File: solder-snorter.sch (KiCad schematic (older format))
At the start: 15 parts, among them J1 USB_B_Micro, M1 Fan, U1 MCP73831, U2 TLV61046A

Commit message: Footprints done; layout started
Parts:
- removed SW?: SW_SPST, symbol Switch:SW_SPST
- added SW1: SW_SPDT, solder-snorter:SW_SPDT_OS102011MA1QN1, symbol Switch:SW_SPDT
- BT1: footprint (none) -> solder-snorter:BatteryHolder_Keystone_54_1x18650; MPN (none) -> Keystone 54 (x 2)
- C1, C2: footprint (none) -> Capacitor_SMD:C_0805_2012Metric_Pad1.15x1.40mm_HandSolder; MPN (none) -> 0805X475M250CT
- C3: footprint (none) -> Capacitor_SMD:C_0805_2012Metric_Pad1.15x1.40mm_HandSolder; MPN (none) -> 0805X225M160CT
- C4: footprint (none) -> Capacitor_SMD:C_0805_2012Metric_Pad1.15x1.40mm_HandSolder; MPN (none) -> C0805C106K4PAC
- D1, D2: footprint (none) -> LED_SMD:LED_0805_2012Metric_Pad1.15x1.40mm_HandSolder
- J1: footprint (none) -> solder-snorter:USB_Micro-B_Amphenol_10118194-0001LF; MPN (none) -> 10118194-0001LF
- L1: footprint (none) -> solder-snorter:L_Murata_FDSD0420-H-100M; MPN (none) -> FDSD0420-H-100M=P3
- M1: footprint (none) -> Connector_PinSocket_2.54mm:PinSocket_1x02_P2.54mm_Vertical; MPN (none) -> CFM-8025V-132-330
- R1, R2: footprint (none) -> Resistor_SMD:R_0805_2012Metric_Pad1.15x1.40mm_HandSolder
- U1: footprint (none) -> Package_TO_SOT_SMD:SOT-23-5_HandSoldering; MPN (none) -> MCP73831T-2ACI/OT
- U2: footprint (none) -> Package_TO_SOT_SMD:SOT-23-6_Handsoldering; MPN (none) -> TLV61046ADBVR
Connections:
- net GND: no longer J1.6 (Shield)
- net VBAT: now also SW1.2 (B)
- net VBATSW: now also SW1.3 (C)
- no-connect marks 3 -> 4
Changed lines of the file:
@@
 F 0 "U1" H 4550 1940 50  0000 C CNN
 F 1 "MCP73831" H 4550 1849 50  0000 C CNN
-F 2 "" H 4550 1475 50  0001 C CNN
-F 3 "" H 4550 1475 50  0001 C CNN
+F 2 "Package_TO_SOT_SMD:SOT-23-5_HandSoldering" H 4550 1475 50  0001 C CNN
+F 3 "https://www.mouser.at/datasheet/2/268/20001984g-846362.pdf" H 4550 1475 50  0001 C CNN
+F 4 "MCP73831T-2ACI/OT" H 4550 1475 50  0001 C CNN "MPN"
 	1    4550 1475
 	1    0    0    -1
@@
 F 0 "J1" H 2307 1942 50  0000 C CNN
 F 1 "USB_B_Micro" H 2307 1851 50  0000 C CNN
-F 2 "" H 2400 1425 50  0001 C CNN
-F 3 "~" H 2400 1425 50  0001 C CNN
+F 2 "solder-snorter:USB_Micro-B_Amphenol_10118194-0001LF" H 2400 1425 50  0001 C CNN
+F 3 "https://cdn.amphenol-icc.com/media/wysiwyg/files/drawing/10118194.pdf" H 2400 1425 50  0001 C CNN
+F 4 "10118194-0001LF" H 2250 1475 50  0001 C CNN "MPN"
 	1    2250 1475
 	1    0    0    -1
@@
 	1    0    0    -1
 $EndComp
-Wire Wire Line
-	2250 1875 2250 1925
-Wire Wire Line
-	2150 1875 2150 1925
-Wire Wire Line
-	2150 1925 2250 1925
-Connection ~ 2250 1925
-Wire Wire Line
-	2250 1925 2250 2025
 NoConn ~ 2550 1475
 NoConn ~ 2550 1575
@@
 F 0 "C1" H 3065 1696 50  0000 L CNN
 F 1 "4.7U" H 3065 1605 50  0000 L CNN
-F 2 "" H 2988 1500 50  0001 C CNN
-F 3 "~" H 2950 1650 50  0001 C CNN
+F 2 "Capacitor_SMD:C_0805_2012Metric_Pad1.15x1.40mm_HandSolder" H 2988 1500 50  0001 C CNN
+F 3 "https://www.mouser.at/datasheet/2/210/WTC_MLCC_General_Purpose-1534899.pdf" H 2950 1650 50  0001 C CNN
+F 4 "0805X475M250CT" H 2950 1650 50  0001 C CNN "MPN"
 	1    2950 1650
 	1    0    0    -1
@@
 F 0 "BT1" H 6343 1646 50  0000 L CNN
 F 1 "Battery_Cell" H 6343 1555 50  0000 L CNN
-F 2 "" V 6225 1610 50  0001 C CNN
-F 3 "~" V 6225 1610 50  0001 C CNN
+F 2 "solder-snorter:BatteryHolder_Keystone_54_1x18650" V 6225 1610 50  0001 C CNN
+F 3 "https://www.mouser.at/datasheet/2/215/4-745936.pdf" V 6225 1610 50  0001 C CNN
+F 4 "Keystone 54 (x 2)" H 6225 1550 50  0001 C CNN "MPN"
 	1    6225 1550
 	1    0    0    -1
@@
 F 0 "R2" H 5245 1771 50  0000 L CNN
 F 1 "2K" H 5245 1680 50  0000 L CNN
-F 2 "" V 5105 1725 50  0001 C CNN
+F 2 "Resistor_SMD:R_0805_2012Metric_Pad1.15x1.40mm_HandSolder" V 5105 1725 50  0001 C CNN
 F 3 "~" H 5175 1725 50  0001 C CNN
 	1    5175 1725
@@
 F 0 "D1" H 3725 1450 50  0000 C CNN
 F 1 "LED" H 3700 1525 50  0000 C CNN
-F 2 "" H 3550 1575 50  0001 C CNN
+F 2 "LED_SMD:LED_0805_2012Metric_Pad1.15x1.40mm_HandSolder" H 3550 1575 50  0001 C CNN
 F 3 "~" H 3550 1575 50  0001 C CNN
 	1    3550 1575
@@
 F 0 "D2" H 3675 1750 50  0000 C CNN
 F 1 "LED" H 3700 1675 50  0000 C CNN
-F 2 "" H 3550 1800 50  0001 C CNN
+F 2 "LED_SMD:LED_0805_2012Metric_Pad1.15x1.40mm_HandSolder" H 3550 1800 50  0001 C CNN
 F 3 "~" H 3550 1800 50  0001 C CNN
 	1    3550 1800
@@
 F 0 "R1" V 3768 1675 50  0000 C CNN
 F 1 "470" V 3859 1675 50  0000 C CNN
-F 2 "" V 3905 1675 50  0001 C CNN
+F 2 "Resistor_SMD:R_0805_2012Metric_Pad1.15x1.40mm_HandSolder" V 3905 1675 50  0001 C CNN
 F 3 "~" H 3975 1675 50  0001 C CNN
 	1    3975 1675
@@
 F 0 "C2" H 5665 1696 50  0000 L CNN
 F 1 "4.7U" H 5665 1605 50  0000 L CNN
-F 2 "" H 5588 1500 50  0001 C CNN
-F 3 "~" H 5550 1650 50  0001 C CNN
+F 2 "Capacitor_SMD:C_0805_2012Metric_Pad1.15x1.40mm_HandSolder" H 5588 1500 50  0001 C CNN
+F 3 "https://www.mouser.at/datasheet/2/210/WTC_MLCC_General_Purpose-1534899.pdf" H 5550 1650 50  0001 C CNN
+F 4 "0805X475M250CT" H 5550 1650 50  0001 C CNN "MPN"
 	1    5550 1650
 	1    0    0    -1
@@
 F 0 "L1" V 4715 3575 50  0000 C CNN
 F 1 "10U" V 4624 3575 50  0000 C CNN
-F 2 "" H 4525 3575 50  0001 C CNN
-F 3 "~" H 4525 3575 50  0001 C CNN
+F 2 "solder-snorter:L_Murata_FDSD0420-H-100M" H 4525 3575 50  0001 C CNN
+F 3 "https://search.murata.co.jp/Ceramy/image/img/P02/J(E)TE243B-0001_FDSD0420_reference.pdf" H 4525 3575 50  0001 C CNN
+F 4 "FDSD0420-H-100M=P3" H 4525 3575 50  0001 C CNN "MPN"
 	1    4525 3575
 	0    -1   -1   0
@@
 F 0 "C3" H 3665 4521 50  0000 L CNN
 F 1 "2.2U" H 3665 4430 50  0000 L CNN
-F 2 "" H 3588 4325 50  0001 C CNN
-F 3 "~" H 3550 4475 50  0001 C CNN
+F 2 "Capacitor_SMD:C_0805_2012Metric_Pad1.15x1.40mm_HandSolder" H 3588 4325 50  0001 C CNN
+F 3 "https://www.mouser.at/datasheet/2/210/WTC_MLCC_General_Purpose-1534899.pdf" H 3550 4475 50  0001 C CNN
+F 4 "0805X225M160CT" H 3550 4475 50  0001 C CNN "MPN"
 	1    3550 4475
 	1    0    0    -1
@@
 F 0 "C4" H 5465 4521 50  0000 L CNN
 F 1 "10U" H 5465 4430 50  0000 L CNN
-F 2 "" H 5388 4325 50  0001 C CNN
-F 3 "~" H 5350 4475 50  0001 C CNN
+F 2 "Capacitor_SMD:C_0805_2012Metric_Pad1.15x1.40mm_HandSolder" H 5388 4325 50  0001 C CNN
+F 3 "https://www.mouser.at/datasheet/2/212/KEM_C1006_X5R_SMD-1103249.pdf" H 5350 4475 50  0001 C CNN
+F 4 "C0805C106K4PAC" H 5350 4475 50  0001 C CNN "MPN"
 	1    5350 4475
 	1    0    0    -1
@@
 F 0 "U2" H 4525 4715 50  0000 C CNN
 F 1 "TLV61046A" H 4525 4624 50  0000 C CNN
-F 2 "" H 4525 4250 79  0001 C CNN
-F 3 "" H 4525 4250 79  0001 C CNN
+F 2 "Package_TO_SOT_SMD:SOT-23-6_Handsoldering" H 4525 4250 79  0001 C CNN
+F 3 "http://www.ti.com/general/docs/suppproductinfo.tsp?distId=26&gotoUrl=http%3A%2F%2Fwww.ti.com%2Flit%2Fds%2Fsymlink%2Ftlv61046a.pdf" H 4525 4250 79  0001 C CNN
+F 4 "TLV61046ADBVR" H 4525 4250 50  0001 C CNN "MPN"
 	1    4525 4250
 	1    0    0    -1
@@
 F 0 "M1" H 8833 4996 50  0000 L CNN
 F 1 "Fan" H 8833 4905 50  0000 L CNN
-F 2 "" H 8675 4910 50  0001 C CNN
-F 3 "~" H 8675 4910 50  0001 C CNN
+F 2 "Connector_PinSocket_2.54mm:PinSocket_1x02_P2.54mm_Vertical" H 8675 4910 50  0001 C CNN
+F 3 "https://www.mouser.at/datasheet/2/670/cfm-80v-1776226.pdf" H 8675 4910 50  0001 C CNN
+F 4 "CFM-8025V-132-330" H 8675 4900 50  0001 C CNN "MPN"
 	1    8675 4900
 	1    0    0    -1
@@
 Text Notes 5175 3625 0    50   ~ 0
 Set up for fixed 12V DC operation
-$Comp
-L Switch:SW_SPST SW?
-U 1 1 5EBDD2BC
-P 2750 6375
-F 0 "SW?" H 2750 6610 50  0000 C CNN
-F 1 "SW_SPST" H 2750 6519 50  0000 C CNN
-F 2 "" H 2750 6375 50  0001 C CNN
-F 3 "~" H 2750 6375 50  0001 C CNN
-	1    2750 6375
-	1    0    0    -1
-$EndComp
-Text GLabel 3150 6375 2    50   Input ~ 0
+Text GLabel 3150 6475 2    50   Input ~ 0
 VBATSW
 Wire Wire Line
-	3150 6375 2950 6375
+	3150 6475 2950 6475
 Text GLabel 2350 6375 0    50   Input ~ 0
 VBAT
@@
 Text Notes 7025 3400 0    50   ~ 0
 Another "copy the datasheet" setup. The TLV61046A has a nice simplified\nsetup for 12V operation, which is what's needed for the fan here.
+Wire Wire Line
+	2250 1875 2250 2025
+NoConn ~ 2150 1875
+$Comp
+L Switch:SW_SPDT SW1
+U 1 1 5EC07698
+P 2750 6375
+F 0 "SW1" H 2750 6660 50  0000 C CNN
+F 1 "SW_SPDT" H 2750 6569 50  0000 C CNN
+F 2 "solder-snorter:SW_SPDT_OS102011MA1QN1" H 2750 6375 50  0001 C CNN
+F 3 "https://www.mouser.at/datasheet/2/60/os-1841429.pdf" H 2750 6375 50  0001 C CNN
+F 4 "OS102011MA1QN1" H 2750 6375 50  0001 C CNN "MPN"
+	1    2750 6375
+	1    0    0    -1
+$EndComp
 $EndSCHEMATC

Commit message: Finished v1.0 layout
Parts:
- added J2, J3: Conn_01x01, MountingHole:MountingHole_4.3mm_M4_DIN965, symbol Connector_Generic:Conn_01x01
- added TP1: GND, TestPoint:TestPoint_Pad_2.0x2.0mm, symbol Connector:TestPoint
- added TP2: VBUS, TestPoint:TestPoint_Pad_2.0x2.0mm, symbol Connector:TestPoint
- added TP3: SW, TestPoint:TestPoint_Pad_2.0x2.0mm, symbol Connector:TestPoint
- added TP4: VBAT, TestPoint:TestPoint_Pad_2.0x2.0mm, symbol Connector:TestPoint
- added TP5: +12V, TestPoint:TestPoint_Pad_2.0x2.0mm, symbol Connector:TestPoint
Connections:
- net +12V: now also TP5.1
- net GND: now also TP1.1
- net VBAT: now also TP4.1
- net at C1.1, D1.2 (A), J1.1 (VBUS)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: now also TP2.1
- net at L1.2, U2.1 (SW): now also TP3.1
- no-connect marks 4 -> 7
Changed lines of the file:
@@
 	3275 1575 3275 1275
 Connection ~ 3275 1275
-Wire Wire Line
-	3275 1275 4200 1275
 $Comp
 L power:GND #PWR02
@@
 $EndComp
 Wire Wire Line
-	4900 1275 5550 1275
+	4900 1275 5150 1275
 Wire Wire Line
 	5550 1500 5550 1275
@@
 	5025 4450 5025 4725
 Wire Wire Line
-	4875 4250 5350 4250
+	4875 4250 5175 4250
 Wire Wire Line
 	5350 4325 5350 4250
@@
 	1    0    0    -1
 $EndComp
+$Comp
+L Connector:TestPoint TP2
+U 1 1 5EC2956E
+P 3900 1275
+F 0 "TP2" H 3958 1393 50  0000 L CNN
+F 1 "VBUS" H 3950 1475 50  0000 L CNN
+F 2 "TestPoint:TestPoint_Pad_2.0x2.0mm" H 4100 1275 50  0001 C CNN
+F 3 "~" H 4100 1275 50  0001 C CNN
+	1    3900 1275
+	1    0    0    -1
+$EndComp
+$Comp
+L Connector:TestPoint TP4
+U 1 1 5EC29D29
+P 5150 1275
+F 0 "TP4" H 5208 1393 50  0000 L CNN
+F 1 "VBAT" H 5200 1475 50  0000 L CNN
+F 2 "TestPoint:TestPoint_Pad_2.0x2.0mm" H 5350 1275 50  0001 C CNN
+F 3 "~" H 5350 1275 50  0001 C CNN
+	1    5150 1275
+	1    0    0    -1
+$EndComp
+Connection ~ 5150 1275
+Wire Wire Line
+	5150 1275 5550 1275
+Connection ~ 3900 1275
+Wire Wire Line
+	3900 1275 4200 1275
+Wire Wire Line
+	3275 1275 3900 1275
+$Comp
+L Connector:TestPoint TP5
+U 1 1 5EC2AF2B
+P 5175 4250
+F 0 "TP5" H 5233 4368 50  0000 L CNN
+F 1 "+12V" H 5225 4450 50  0000 L CNN
+F 2 "TestPoint:TestPoint_Pad_2.0x2.0mm" H 5375 4250 50  0001 C CNN
+F 3 "~" H 5375 4250 50  0001 C CNN
+	1    5175 4250
+	1    0    0    -1
+$EndComp
+Connection ~ 5175 4250
+Wire Wire Line
+	5175 4250 5350 4250
+$Comp
+L Connector:TestPoint TP3
+U 1 1 5EC2B370
+P 4950 3575
+F 0 "TP3" H 5008 3693 50  0000 L CNN
+F 1 "SW" H 5000 3775 50  0000 L CNN
+F 2 "TestPoint:TestPoint_Pad_2.0x2.0mm" H 5150 3575 50  0001 C CNN
+F 3 "~" H 5150 3575 50  0001 C CNN
+	1    4950 3575
+	1    0    0    -1
+$EndComp
+Connection ~ 4950 3575
+$Comp
+L Connector:TestPoint TP1
+U 1 1 5EC2BF46
+P 2950 1975
+F 0 "TP1" H 3008 2093 50  0000 L CNN
+F 1 "GND" H 3000 2175 50  0000 L CNN
+F 2 "TestPoint:TestPoint_Pad_2.0x2.0mm" H 3150 1975 50  0001 C CNN
+F 3 "~" H 3150 1975 50  0001 C CNN
+	1    2950 1975
+	-1   0    0    1
+$EndComp
+Connection ~ 2950 1975
+NoConn ~ 2950 6275
+$Comp
+L Connector_Generic:Conn_01x01 J2
+U 1 1 5EC47C3E
+P 8775 1750
+F 0 "J2" H 8855 1792 50  0000 L CNN
+F 1 "Conn_01x01" H 8855 1701 50  0000 L CNN
+F 2 "MountingHole:MountingHole_4.3mm_M4_DIN965" H 8775 1750 50  0001 C CNN
+F 3 "~" H 8775 1750 50  0001 C CNN
+	1    8775 1750
+	1    0    0    -1
+$EndComp
+$Comp
+L Connector_Generic:Conn_01x01 J3
+U 1 1 5EC496C7
+P 8775 1975
+F 0 "J3" H 8855 2017 50  0000 L CNN
+F 1 "Conn_01x01" H 8855 1926 50  0000 L CNN
+F 2 "MountingHole:MountingHole_4.3mm_M4_DIN965" H 8775 1975 50  0001 C CNN
+F 3 "~" H 8775 1975 50  0001 C CNN
+	1    8775 1975
+	1    0    0    -1
+$EndComp
+NoConn ~ 8575 1975
+NoConn ~ 8575 1750
 $EndSCHEMATC

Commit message: v1.0 finished
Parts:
- R1: MPN (none) -> CRCW0805470RFKEAC
- R2: MPN (none) -> CRCW08052K00FKEAC
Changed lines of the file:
@@
 F 1 "2K" H 5245 1680 50  0000 L CNN
 F 2 "Resistor_SMD:R_0805_2012Metric_Pad1.15x1.40mm_HandSolder" V 5105 1725 50  0001 C CNN
-F 3 "~" H 5175 1725 50  0001 C CNN
+F 3 "https://www.mouser.at/datasheet/2/427/crcwce3-1762584.pdf" H 5175 1725 50  0001 C CNN
+F 4 "CRCW08052K00FKEAC" H 5175 1725 50  0001 C CNN "MPN"
 	1    5175 1725
 	1    0    0    -1
@@
 F 1 "470" V 3859 1675 50  0000 C CNN
 F 2 "Resistor_SMD:R_0805_2012Metric_Pad1.15x1.40mm_HandSolder" V 3905 1675 50  0001 C CNN
-F 3 "~" H 3975 1675 50  0001 C CNN
+F 3 "https://www.mouser.at/datasheet/2/427/crcwce3-1762584.pdf" H 3975 1675 50  0001 C CNN
+F 4 "CRCW0805470RFKEAC" H 3975 1675 50  0001 C CNN "MPN"
 	1    3975 1675
 	0    1    1    0

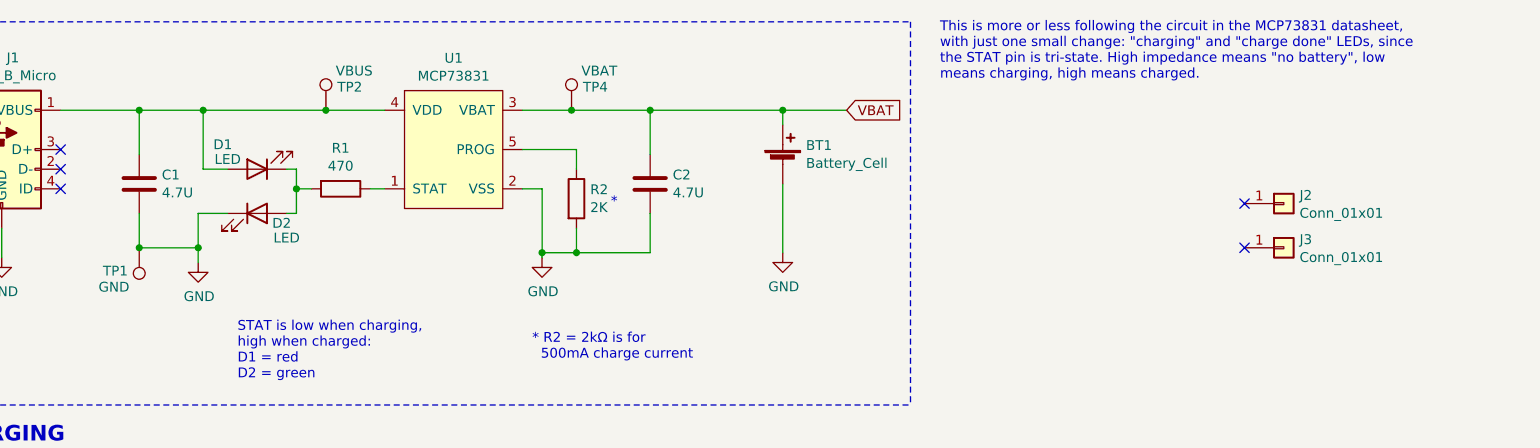
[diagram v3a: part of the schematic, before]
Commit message: Fix LED resistor mistake
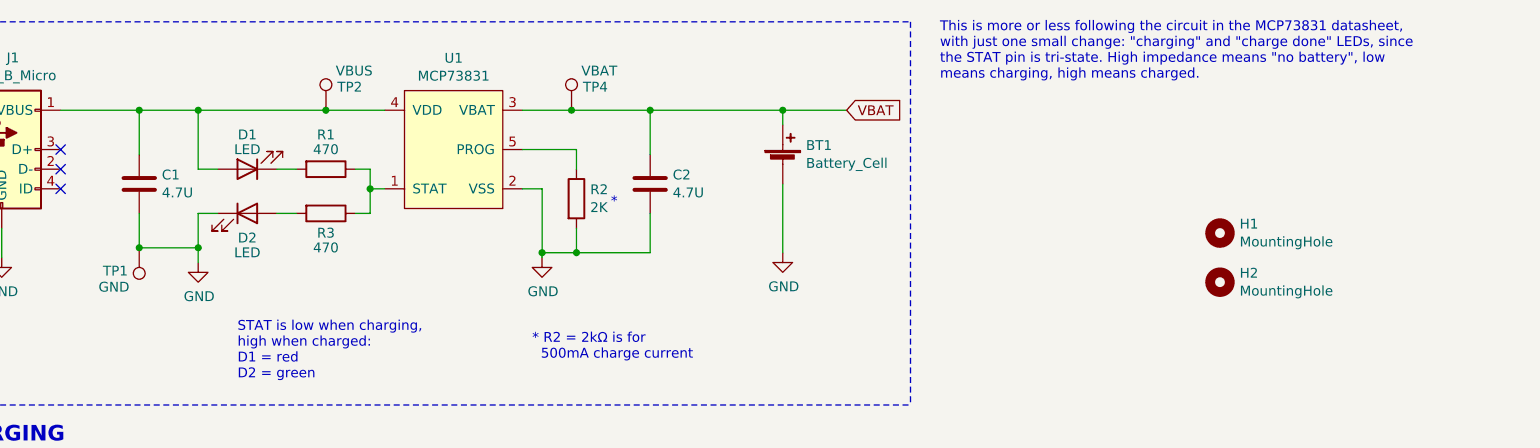
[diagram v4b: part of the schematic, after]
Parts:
- removed J2, J3: Conn_01x01, MountingHole:MountingHole_4.3mm_M4_DIN965, symbol Connector_Generic:Conn_01x01
- added H1, H2: MountingHole, MountingHole:MountingHole_4.3mm_M4_DIN965, symbol Mechanical:MountingHole
- added R3: 470, Resistor_SMD:R_0805_2012Metric_Pad1.15x1.40mm_HandSolder, symbol Device:R
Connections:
- net at R1.1, U1.1 (STAT): now also R3.1
- net at D1.1 (K), R1.2: no longer D2.2 (A)
- new net: D2.2 (A), R3.2
- no-connect marks 7 -> 5
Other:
- moved on the sheet: D1, D2, R1
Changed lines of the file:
@@
 L Device:LED D1
 U 1 1 5EBB3A5D
-P 3550 1575
-F 0 "D1" H 3725 1450 50  0000 C CNN
-F 1 "LED" H 3700 1525 50  0000 C CNN
-F 2 "LED_SMD:LED_0805_2012Metric_Pad1.15x1.40mm_HandSolder" H 3550 1575 50  0001 C CNN
-F 3 "~" H 3550 1575 50  0001 C CNN
-	1    3550 1575
+P 3500 1575
+F 0 "D1" H 3500 1400 50  0000 C CNN
+F 1 "LED" H 3500 1475 50  0000 C CNN
+F 2 "LED_SMD:LED_0805_2012Metric_Pad1.15x1.40mm_HandSolder" H 3500 1575 50  0001 C CNN
+F 3 "~" H 3500 1575 50  0001 C CNN
+	1    3500 1575
 	-1   0    0    1
 $EndComp
@@
 L Device:LED D2
 U 1 1 5EBB48F6
-P 3550 1800
-F 0 "D2" H 3675 1750 50  0000 C CNN
-F 1 "LED" H 3700 1675 50  0000 C CNN
-F 2 "LED_SMD:LED_0805_2012Metric_Pad1.15x1.40mm_HandSolder" H 3550 1800 50  0001 C CNN
-F 3 "~" H 3550 1800 50  0001 C CNN
-	1    3550 1800
+P 3500 1800
+F 0 "D2" H 3500 1675 50  0000 C CNN
+F 1 "LED" H 3500 1600 50  0000 C CNN
+F 2 "LED_SMD:LED_0805_2012Metric_Pad1.15x1.40mm_HandSolder" H 3500 1800 50  0001 C CNN
+F 3 "~" H 3500 1800 50  0001 C CNN
+	1    3500 1800
 	1    0    0    -1
 $EndComp
@@
 L Device:R R1
 U 1 1 5EBB92B4
-P 3975 1675
-F 0 "R1" V 3768 1675 50  0000 C CNN
-F 1 "470" V 3859 1675 50  0000 C CNN
-F 2 "Resistor_SMD:R_0805_2012Metric_Pad1.15x1.40mm_HandSolder" V 3905 1675 50  0001 C CNN
-F 3 "https://www.mouser.at/datasheet/2/427/crcwce3-1762584.pdf" H 3975 1675 50  0001 C CNN
-F 4 "CRCW0805470RFKEAC" H 3975 1675 50  0001 C CNN "MPN"
-	1    3975 1675
+P 3900 1575
+F 0 "R1" V 3725 1575 50  0000 C CNN
+F 1 "470" V 3800 1575 50  0000 C CNN
+F 2 "Resistor_SMD:R_0805_2012Metric_Pad1.15x1.40mm_HandSolder" V 3830 1575 50  0001 C CNN
+F 3 "https://www.mouser.at/datasheet/2/427/crcwce3-1762584.pdf" H 3900 1575 50  0001 C CNN
+F 4 "CRCW0805470RFKEAC" H 3900 1575 50  0001 C CNN "MPN"
+	1    3900 1575
 	0    1    1    0
 $EndComp
@@
 	4125 1675 4200 1675
 Wire Wire Line
-	3825 1675 3750 1675
-Wire Wire Line
-	3750 1675 3750 1575
-Wire Wire Line
-	3750 1575 3700 1575
-Wire Wire Line
-	3700 1800 3750 1800
-Wire Wire Line
-	3750 1800 3750 1675
-Connection ~ 3750 1675
-Wire Wire Line
 	2550 1275 2950 1275
-Wire Wire Line
-	3400 1575 3275 1575
-Wire Wire Line
-	3275 1575 3275 1275
-Connection ~ 3275 1275
 $Comp
 L power:GND #PWR02
@@
 $EndComp
 Wire Wire Line
-	3400 1800 3250 1800
-Wire Wire Line
 	3250 1800 3250 1975
 Wire Wire Line
 	2950 1500 2950 1275
 Connection ~ 2950 1275
-Wire Wire Line
-	2950 1275 3275 1275
 Wire Wire Line
 	2950 1800 2950 1975
@@
 Wire Wire Line
 	3900 1275 4200 1275
-Wire Wire Line
-	3275 1275 3900 1275
 $Comp
 L Connector:TestPoint TP5
@@
 NoConn ~ 2950 6275
 $Comp
-L Connector_Generic:Conn_01x01 J2
-U 1 1 5EC47C3E
-P 8775 1750
-F 0 "J2" H 8855 1792 50  0000 L CNN
-F 1 "Conn_01x01" H 8855 1701 50  0000 L CNN
-F 2 "MountingHole:MountingHole_4.3mm_M4_DIN965" H 8775 1750 50  0001 C CNN
-F 3 "~" H 8775 1750 50  0001 C CNN
-	1    8775 1750
-	1    0    0    -1
-$EndComp
-$Comp
-L Connector_Generic:Conn_01x01 J3
-U 1 1 5EC496C7
-P 8775 1975
-F 0 "J3" H 8855 2017 50  0000 L CNN
-F 1 "Conn_01x01" H 8855 1926 50  0000 L CNN
-F 2 "MountingHole:MountingHole_4.3mm_M4_DIN965" H 8775 1975 50  0001 C CNN
-F 3 "~" H 8775 1975 50  0001 C CNN
-	1    8775 1975
-	1    0    0    -1
-$EndComp
-NoConn ~ 8575 1975
-NoConn ~ 8575 1750
+L Device:R R3
+U 1 1 5ED56DDF
+P 3900 1800
+F 0 "R3" V 4000 1800 50  0000 C CNN
+F 1 "470" V 4075 1800 50  0000 C CNN
+F 2 "Resistor_SMD:R_0805_2012Metric_Pad1.15x1.40mm_HandSolder" V 3830 1800 50  0001 C CNN
+F 3 "https://www.mouser.at/datasheet/2/427/crcwce3-1762584.pdf" H 3900 1800 50  0001 C CNN
+F 4 "CRCW0805470RFKEAC" H 3900 1800 50  0001 C CNN "MPN"
+	1    3900 1800
+	0    1    1    0
+$EndComp
+Wire Wire Line
+	4050 1575 4125 1575
+Wire Wire Line
+	4125 1575 4125 1675
+Wire Wire Line
+	4125 1800 4050 1800
+Connection ~ 4125 1675
+Wire Wire Line
+	4125 1675 4125 1800
+Wire Wire Line
+	2950 1275 3250 1275
+Wire Wire Line
+	3250 1800 3350 1800
+Wire Wire Line
+	3350 1575 3250 1575
+Wire Wire Line
+	3250 1575 3250 1275
+Connection ~ 3250 1275
+Wire Wire Line
+	3250 1275 3900 1275
+Wire Wire Line
+	3650 1575 3750 1575
+Wire Wire Line
+	3650 1800 3750 1800
+$Comp
+L Mechanical:MountingHole H1
+U 1 1 5ED603EE
+P 8450 1900
+F 0 "H1" H 8550 1946 50  0000 L CNN
+F 1 "MountingHole" H 8550 1855 50  0000 L CNN
+F 2 "MountingHole:MountingHole_4.3mm_M4_DIN965" H 8450 1900 50  0001 C CNN
+F 3 "~" H 8450 1900 50  0001 C CNN
+	1    8450 1900
+	1    0    0    -1
+$EndComp
+$Comp
+L Mechanical:MountingHole H2
+U 1 1 5ED6078F
+P 8450 2150
+F 0 "H2" H 8550 2196 50  0000 L CNN
+F 1 "MountingHole" H 8550 2105 50  0000 L CNN
+F 2 "MountingHole:MountingHole_4.3mm_M4_DIN965" H 8450 2150 50  0001 C CNN
+F 3 "~" H 8450 2150 50  0001 C CNN
+	1    8450 2150
+	1    0    0    -1
+$EndComp
 $EndSCHEMATC
